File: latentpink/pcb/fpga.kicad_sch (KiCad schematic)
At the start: 39 parts, among them J9 XILINX_JTAG, M2 960-23-23-F-AB-0, U2 XC7K160T-2FBG484C

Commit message: Continued initial QDR routing
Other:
- sheet QDR SRAM ports: added none; removed 3V3
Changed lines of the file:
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@@
   (paper "A3")
   (title_block
-    (date "2023-06-01")
+    (date "2023-06-03")
     (rev "0.1")
     (company "Antikernel Labs")
@@
     (effects (font (size 1.27 1.27)) (justify right bottom))
   )
-  (label "3V3" (at 46.99 25.4 0)
-    (effects (font (size 1.27 1.27)) (justify left bottom))
-  )
   (label "GND" (at 96.52 91.44 180)
     (effects (font (size 1.27 1.27)) (justify right bottom))
@@
       (effects (font (size 1.27 1.27)) (justify right))
     )
-    (pin "3V3" input (at 46.99 25.4 0)
-      (effects (font (size 1.27 1.27)) (justify right))
-    )

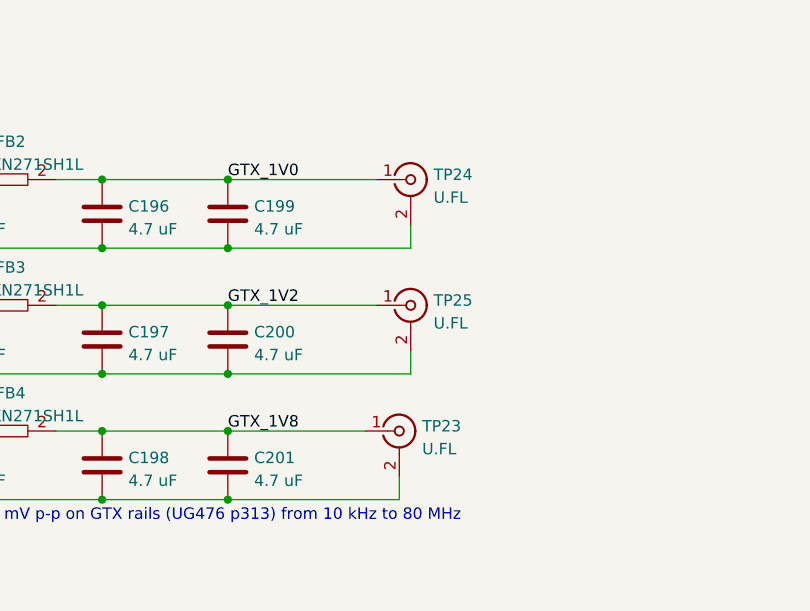
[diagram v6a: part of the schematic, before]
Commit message: Updated schematic with notes on power rail sequencing bug found during bringup
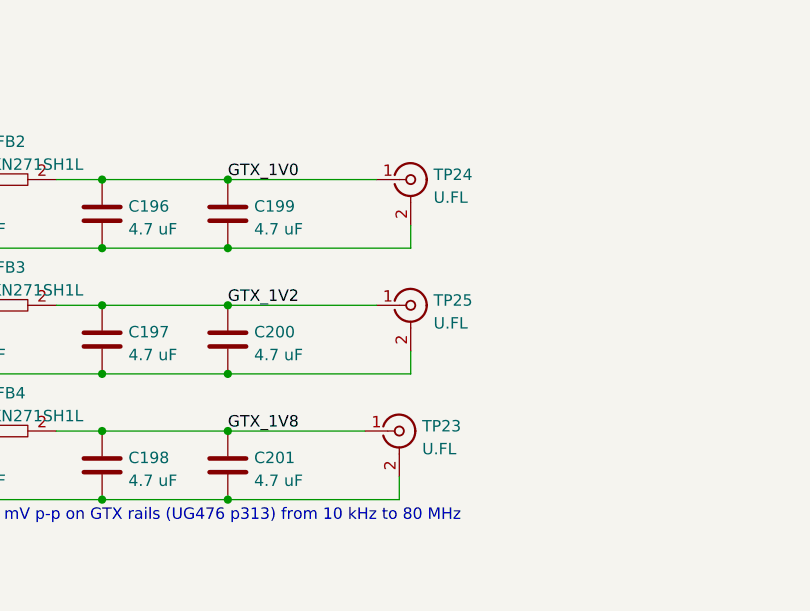
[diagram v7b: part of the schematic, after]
